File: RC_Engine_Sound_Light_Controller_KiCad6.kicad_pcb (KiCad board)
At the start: 2 copper layers, 87.5 x 40.5 mm, 48 parts, among them J1 RX, J10 RGB, J12 CH1, J13 CH2, J14 CH3, J16 CH4, J17 Brushed Motor output, J2 HeadL, J3 TailL, J4 RoofL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

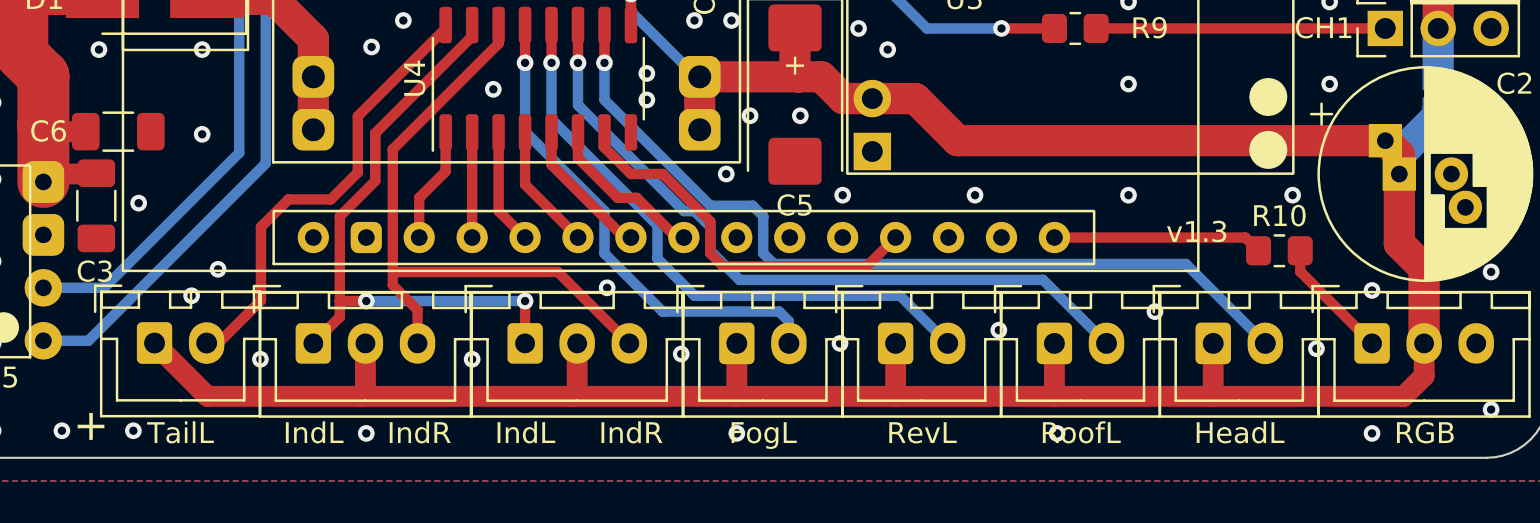
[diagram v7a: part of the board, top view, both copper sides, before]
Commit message: C2 pad traces on front and back.
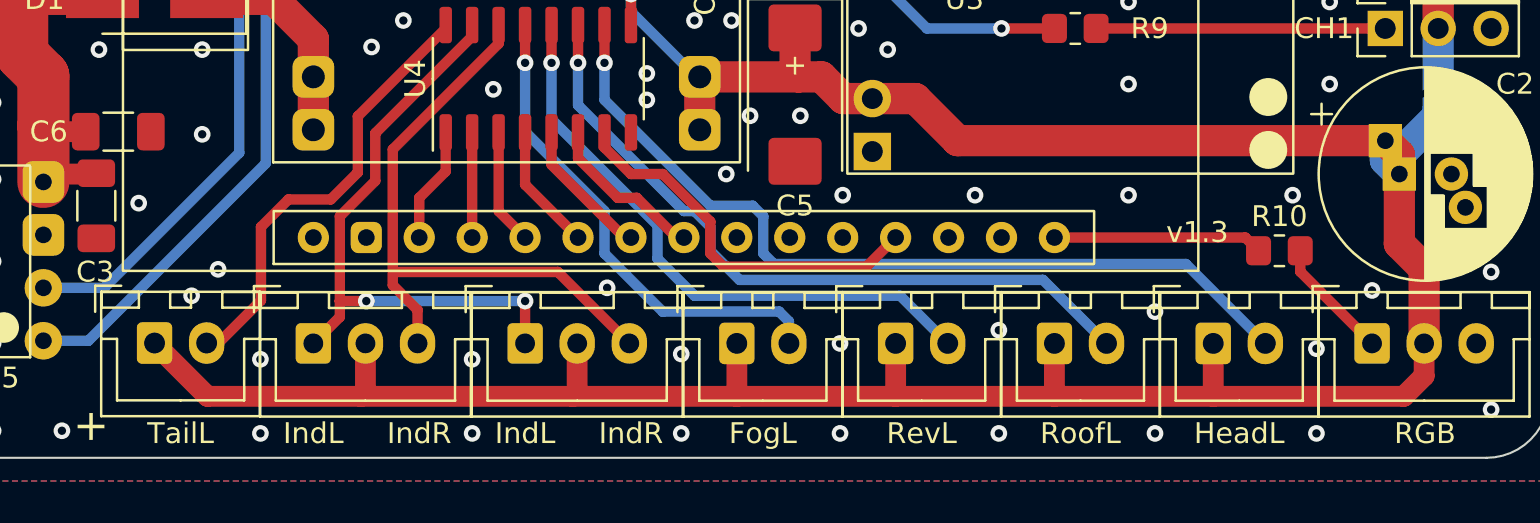
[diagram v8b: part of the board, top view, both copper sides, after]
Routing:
- net VCC: track 138.4 -> 140.3 mm
- net -BATT: vias 94 -> 96
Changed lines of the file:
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@@
   (via (at 80.264 47.752) (size 0.8) (drill 0.4) (layers "F.Cu" "B.Cu") (free) (net 9))
   (via (at 65.532 65.659) (size 0.8) (drill 0.4) (layers "F.Cu" "B.Cu") (free) (net 9))
-  (via (at 84.074 84.201) (size 0.8) (drill 0.4) (layers "F.Cu" "B.Cu") (free) (net 9))
+  (via (at 90.17 84.328) (size 0.8) (drill 0.4) (layers "F.Cu" "B.Cu") (free) (net 9))
   (via (at 77.343 72.136) (size 0.8) (drill 0.4) (layers "F.Cu" "B.Cu") (free) (net 9))
   (via (at 131.826 63.627) (size 0.8) (drill 0.4) (layers "F.Cu" "B.Cu") (free) (net 9))
@@
   (via (at 76.8604 52.07) (size 0.8) (drill 0.4) (layers "F.Cu" "B.Cu") (free) (net 9))
   (via (at 128.905 52.07) (size 0.8) (drill 0.4) (layers "F.Cu" "B.Cu") (free) (net 9))
-  (via (at 143.51 84.328) (size 0.8) (drill 0.4) (layers "F.Cu" "B.Cu") (free) (net 9))
+  (via (at 140.843 84.328) (size 0.8) (drill 0.4) (layers "F.Cu" "B.Cu") (free) (net 9))
   (via (at 83.439 58.42) (size 0.8) (drill 0.4) (layers "F.Cu" "B.Cu") (free) (net 9))
   (via (at 106.299 55.626) (size 0.8) (drill 0.4) (layers "F.Cu" "B.Cu") (free) (net 9))
@@
   (via (at 87.376 65.913) (size 0.8) (drill 0.4) (layers "F.Cu" "B.Cu") (free) (net 9))
   (via (at 133.096 78.486) (size 0.8) (drill 0.4) (layers "F.Cu" "B.Cu") (free) (net 9))
-  (via (at 113.03 84.328) (size 0.8) (drill 0.4) (layers "F.Cu" "B.Cu") (free) (net 9))
+  (via (at 110.363 84.328) (size 0.8) (drill 0.4) (layers "F.Cu" "B.Cu") (free) (net 9))
   (via (at 100.33 80.772) (size 0.8) (drill 0.4) (layers "F.Cu" "B.Cu") (free) (net 9))
   (via (at 131.826 67.564) (size 0.8) (drill 0.4) (layers "F.Cu" "B.Cu") (free) (net 9))
@@
   (via (at 81.915 54.356) (size 0.8) (drill 0.4) (layers "F.Cu" "B.Cu") (free) (net 9))
   (via (at 137.2616 46.1772) (size 0.8) (drill 0.4) (layers "F.Cu" "B.Cu") (free) (net 9))
-  (via (at 128.397 84.328) (size 0.8) (drill 0.4) (layers "F.Cu" "B.Cu") (free) (net 9))
+  (via (at 133.096 84.328) (size 0.8) (drill 0.4) (layers "F.Cu" "B.Cu") (free) (net 9))
   (via (at 70.358 46.228) (size 0.8) (drill 0.4) (layers "F.Cu" "B.Cu") (free) (net 9))
   (via (at 67.31 46.7868) (size 0.8) (drill 0.4) (layers "F.Cu" "B.Cu") (free) (net 9))
   (via (at 121.92 57.404) (size 0.8) (drill 0.4) (layers "F.Cu" "B.Cu") (free) (net 9))
-  (via (at 95.25 84.328) (size 0.8) (drill 0.4) (layers "F.Cu" "B.Cu") (free) (net 9))
+  (via (at 100.33 84.328) (size 0.8) (drill 0.4) (layers "F.Cu" "B.Cu") (free) (net 9))
   (via (at 112.522 71.882) (size 0.8) (drill 0.4) (layers "F.Cu" "B.Cu") (free) (net 9))
   (via (at 102.3 51.7) (size 0.8) (drill 0.4) (layers "F.Cu" "B.Cu") (free) (net 9))
   (via (at 136.525 52.07) (size 0.8) (drill 0.4) (layers "F.Cu" "B.Cu") (free) (net 9))
+  (via (at 117.983 84.328) (size 0.8) (drill 0.4) (layers "F.Cu" "B.Cu") (free) (net 9))
   (via (at 139.7 72.898) (size 0.8) (drill 0.4) (layers "F.Cu" "B.Cu") (free) (net 9))
   (via (at 118.11 72.898) (size 0.8) (drill 0.4) (layers "F.Cu" "B.Cu") (free) (net 9))
   (via (at 149.225 83.185) (size 0.8) (drill 0.4) (layers "F.Cu" "B.Cu") (free) (net 9))
+  (via (at 125.603 84.328) (size 0.8) (drill 0.4) (layers "F.Cu" "B.Cu") (free) (net 9))
   (via (at 141.478 63.627) (size 0.8) (drill 0.4) (layers "F.Cu" "B.Cu") (free) (net 9))
   (via (at 76.835 60.96) (size 0.8) (drill 0.4) (layers "F.Cu" "B.Cu") (free) (net 9))
@@
   (segment (start 146.01 81.574) (end 145.034 82.55) (width 1) (layer "F.Cu") (net 19))
   (segment (start 111.252 67.22) (end 111.252 69.76) (width 1.5) (layer "F.Cu") (net 19))
-  (segment (start 144.82 70.952937) (end 144.149063 70.282) (width 1.5) (layer "F.Cu") (net 19))
   (segment (start 121.6025 68.2625) (end 123.622 70.282) (width 1.5) (layer "F.Cu") (net 19))
   (segment (start 120.65 82.55) (end 113.03 82.55) (width 1) (layer "F.Cu") (net 19))
@@
   (segment (start 105.156 82.55) (end 94.996 82.55) (width 1) (layer "F.Cu") (net 19))
   (segment (start 105.37 80.01) (end 105.37 82.336) (width 1) (layer "F.Cu") (net 19))
+  (segment (start 144.82 70.952937) (end 144.149063 70.282) (width 1.5) (layer "F.Cu") (net 19))
   (segment (start 118.135 68.2625) (end 121.6025 68.2625) (width 1.5) (layer "F.Cu") (net 19))
   (segment (start 144.82 71.882) (end 144.82 70.952937) (width 1.5) (layer "F.Cu") (net 19))
@@
   (segment (start 128.27 80.01) (end 128.27 82.55) (width 1) (layer "F.Cu") (net 19))
   (via (at 107.95 63.246) (size 0.8) (drill 0.4) (layers "F.Cu" "B.Cu") (free) (net 19))
+  (segment locked (start 144.149063 71.211063) (end 144.82 71.882) (width 1.5) (layer "B.Cu") (net 19))
   (segment (start 107.95 64.09) (end 111.08 67.22) (width 0.5) (layer "B.Cu") (net 19))
   (segment (start 146.685 69.088) (end 145.034 70.739) (width 1.5) (layer "B.Cu") (net 19))
   (segment (start 107.95 63.246) (end 107.95 64.09) (width 0.5) (layer "B.Cu") (net 19))
+  (segment locked (start 144.149063 70.282) (end 144.149063 71.211063) (width 1.5) (layer "B.Cu") (net 19))
   (segment (start 146.685 68.728) (end 146.685 69.088) (width 1.5) (layer "B.Cu") (net 19))
   (segment (start 140.065 75.565) (end 140.065 76.565) (width 0.5) (layer "F.Cu") (net 21))
